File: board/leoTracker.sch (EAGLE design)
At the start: 54 parts, among them J1 AVR_SPI_PRG_6PTH, Q1 MOSFET-NCHANNELSMD, U3 ATMEGA32U4, X1 USB-MINIB-5PIN, Y1 16MHz

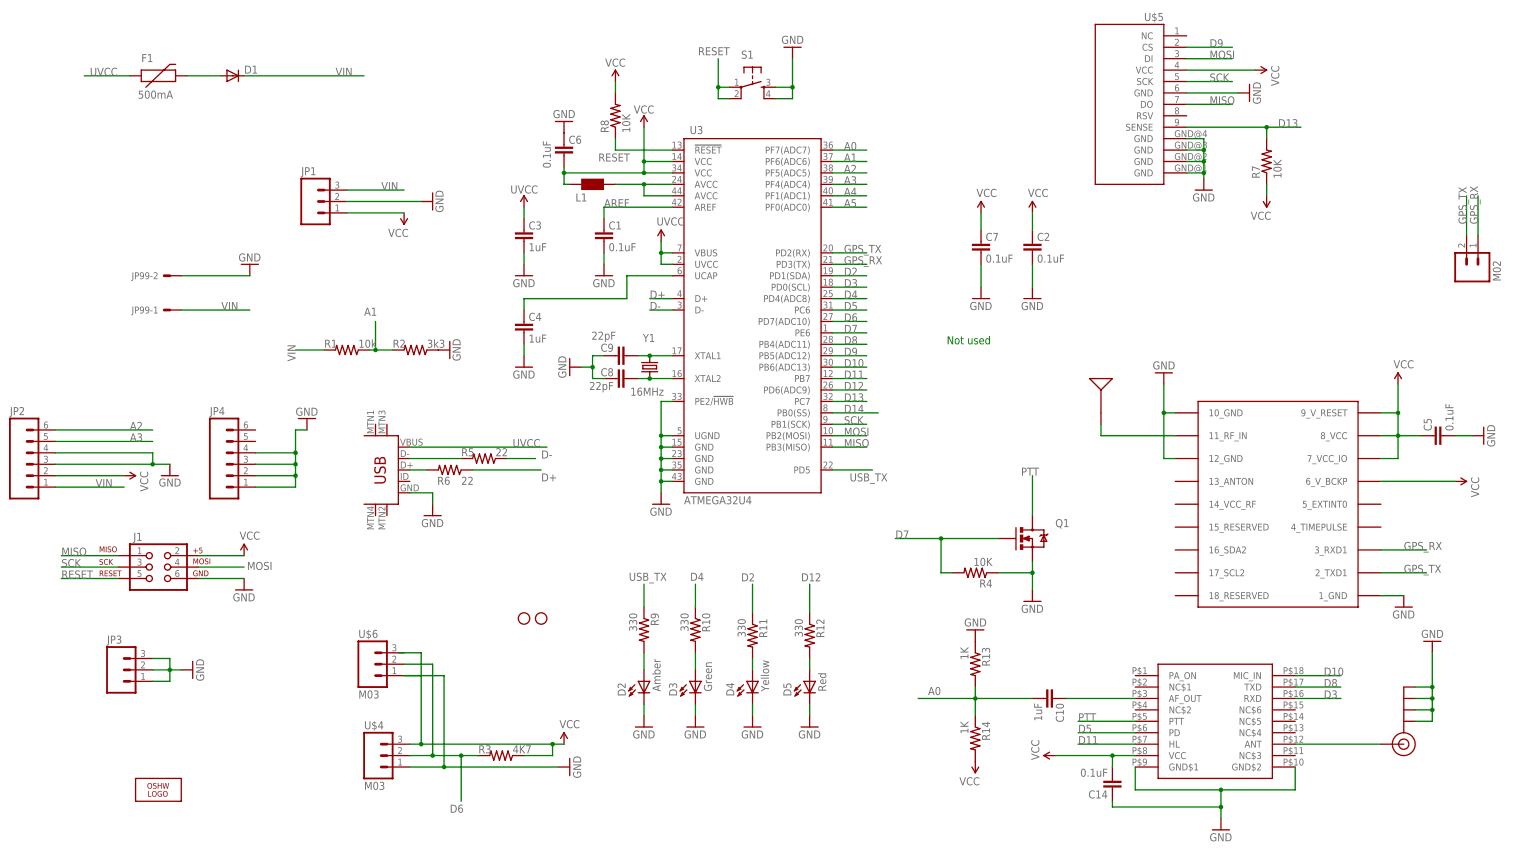
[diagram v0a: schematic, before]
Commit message: Latest version: Used new SA818 footprint; changed crystal; cleaned up silkscreen for fabrication
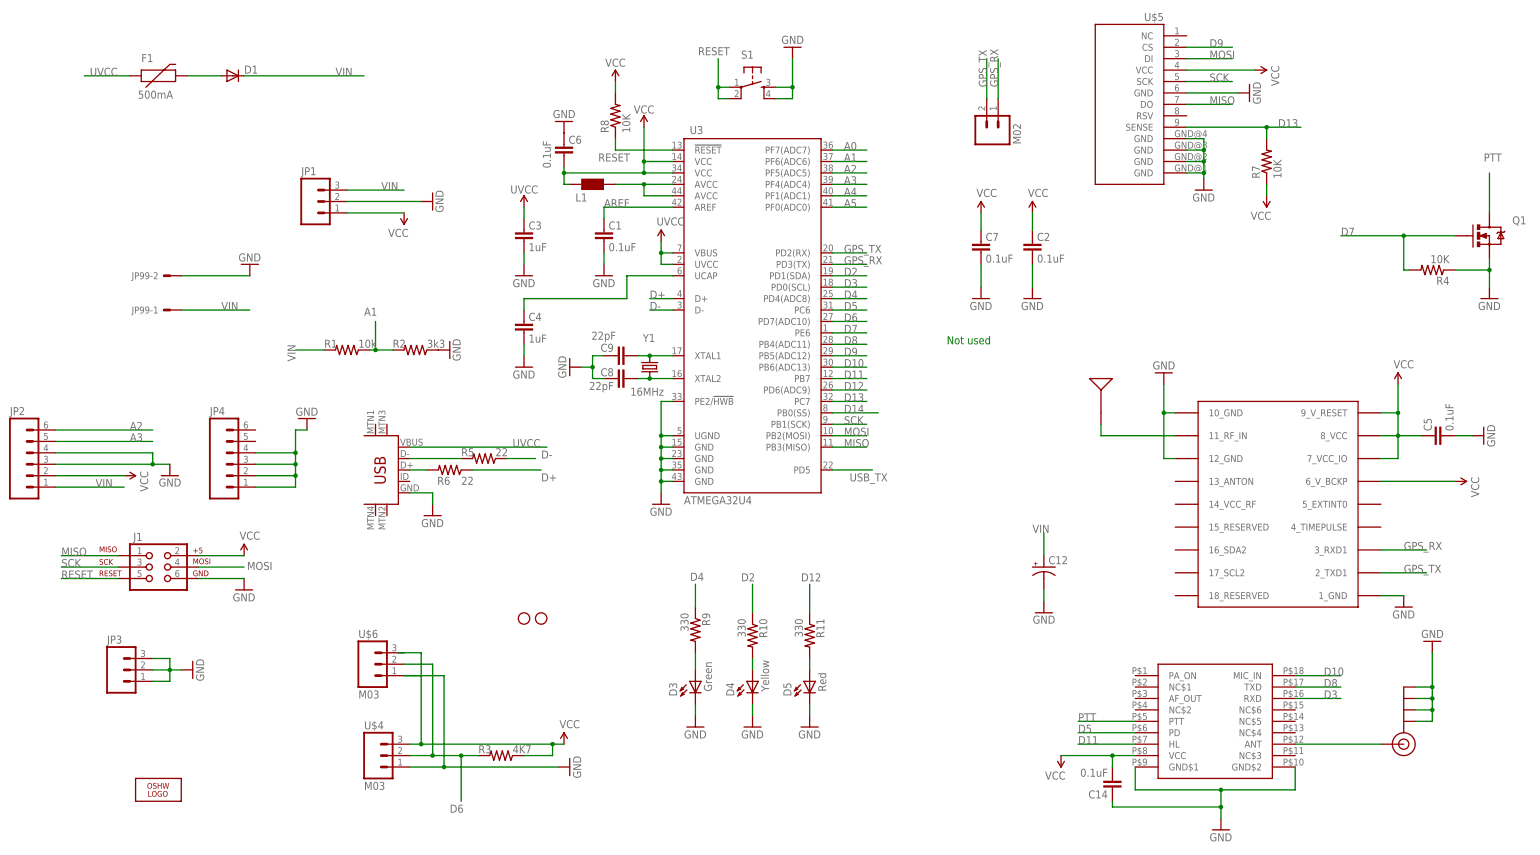
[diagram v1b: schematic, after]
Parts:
- removed C10: 1uF, SparkFun:CAP0805
- removed D2: Amber, SparkFun-LED:LED0603
- removed R12: 330, SparkFun-Passives:RESISTOR0805-RES
- removed R13, R14: 1K, SparkFun-Passives:RESISTOR0805-RES
- added C12: (no value), rcl:CPOL-US153CLV-0405
- U$7: device BLOATEDnicerf:SA818 -> nicerf:SA818
- Y1: device SparkFun:CRYSTAL5X3 -> newAva:ABRACON_ABM3_CRYSTAL
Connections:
- removed net N$16: D2.A, R9.2
- removed net N$9: C10.2, U$7.AF_OUT
- net A0: no longer C10.1, R13.2, R14.1
- net D12: now also R11.1; no longer R12.1
- net D2: now also R10.1; no longer R11.1
- net D4: now also R9.1; no longer R10.1
- net GND: now also C12.-; no longer D2.C, R13.1
- net N$10: now also R11.2; no longer R12.2
- net N$5: now also R9.2; no longer R10.2
- net N$7: now also R10.2; no longer R11.2
- net USB_TX: no longer R9.1
- net VCC: no longer R14.2
- net VIN: now also C12.+
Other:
- moved on the sheet: Q1, R10, R11, R4, R9
